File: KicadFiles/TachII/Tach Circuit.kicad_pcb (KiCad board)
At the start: 2 copper layers, 44.4 x 24.1 mm, 17 parts, among them Q1 2N3904

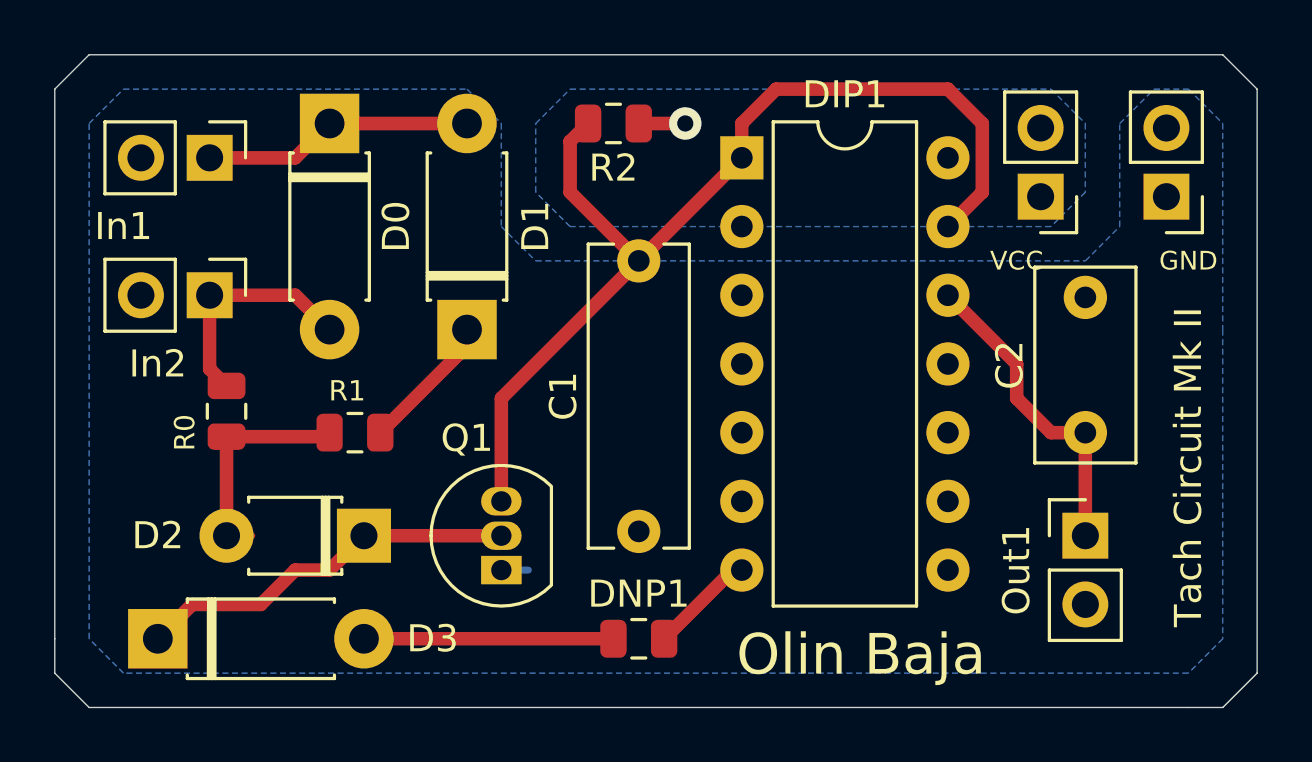
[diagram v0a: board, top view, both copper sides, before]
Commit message: Added logo and fixed connectors
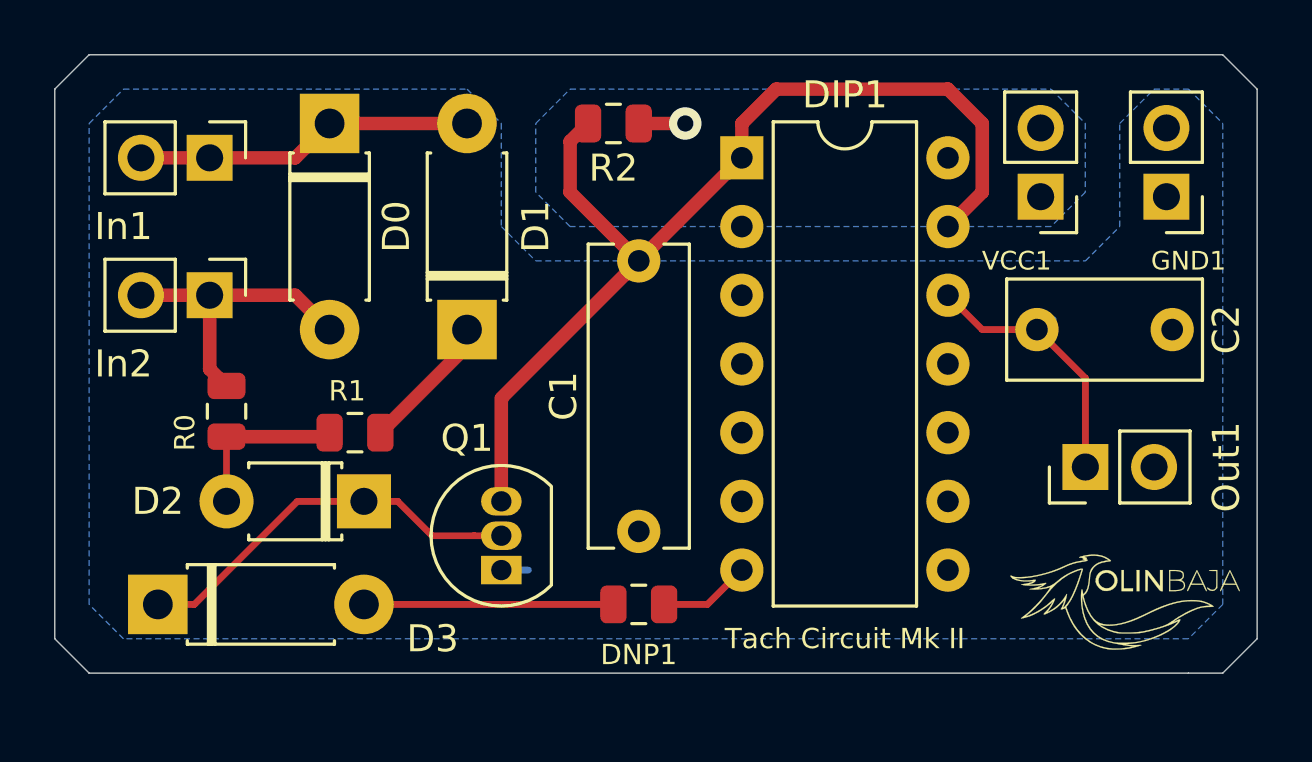
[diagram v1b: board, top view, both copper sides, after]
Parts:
- added G***: LOGO, TestBaja:Baja_Logo_Tach, F.Cu at (163.8, -86.4)
- moved C2 4.21 mm to (159.5, -96.5), turned to 0 degrees
- moved Out1 2.54 mm to (161.3, -91.4), turned to 90 degrees
- moved D2 1.27 mm to (134.6, -90.2)
- moved D3 1.27 mm to (127.0, -86.4)
- moved DNP1 1.27 mm to (144.8, -86.4)
- renumbered GND to GND1, VCC to VCC1
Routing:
- net Net-(D0-Pad2): track 8.57 -> 11.1 mm
- net Net-(D0-Pad1): track 10.0 -> 12.6 mm
- net Net-(D2-Pad2): track 8.47 -> 6.26 mm
- net Net-(C2-Pad1): track 11.7 -> 10.0 mm
- net GND: track 5.30 -> 4.73 mm
- net Net-(D2-Pad1): track 14.3 -> 14.8 mm
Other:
- board size 44.4 x 24.1 mm -> 44.4 x 22.9 mm
- board text removed: "Olin Baja"
